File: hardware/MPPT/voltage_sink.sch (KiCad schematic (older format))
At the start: 8 parts

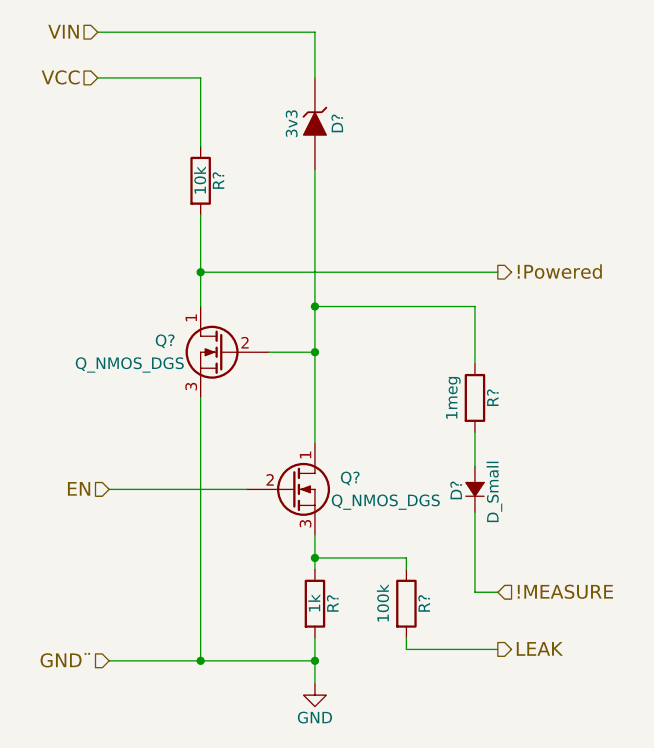
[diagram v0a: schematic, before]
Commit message: Add signaling LEDs to voltage clamps, adjust time constant on peak detect.
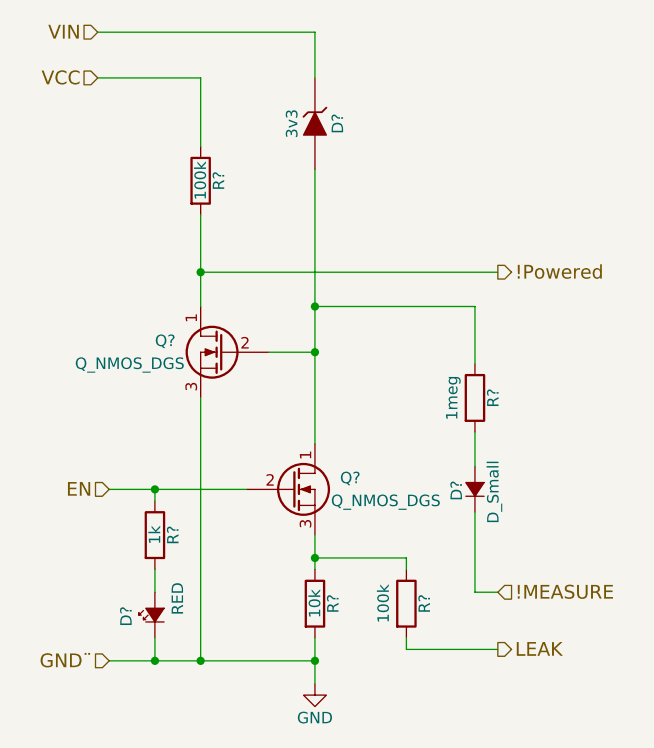
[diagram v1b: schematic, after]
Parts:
- added D?: RED, symbol Led_Small
- added R?: 1k, symbol R
- R?: value 10k -> 100k
- R?: value 1k -> 10k
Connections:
- net EN: now also R?.1
- net GND: now also D?.1 (K)
- new net: D?.2 (A), R?.2
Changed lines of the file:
@@
 $Descr A4 11693 8268
 encoding utf-8
-Sheet 6 7
+Sheet 2 7
 Title ""
 Date ""
@@
 AR Path="/55E4F9FD/55E4BF6F" Ref="D?"  Part="1"
 AR Path="/55E4FA05/55E4BF6F" Ref="D?"  Part="1"
+AR Path="/55E4E347/55E4BF6F" Ref="D?"  Part="1"
 F 0 "D?" H 3000 1650 50  0000 C CNN
 F 1 "3v3" H 3000 1450 50  0000 C CNN
@@
 AR Path="/55E4F9FD/55E4BF9E" Ref="Q?"  Part="1"
 AR Path="/55E4FA05/55E4BF9E" Ref="Q?"  Part="1"
+AR Path="/55E4E347/55E4BF9E" Ref="Q?"  Part="1"
 F 0 "Q?" H 3200 3200 50  0000 R CNN
 F 1 "Q_NMOS_DGS" H 3550 3100 50  0000 R CNN
@@
 AR Path="/55E4F9FD/55E4C1A1" Ref="#PWR?"  Part="1"
 AR Path="/55E4FA05/55E4C1A1" Ref="#PWR?"  Part="1"
+AR Path="/55E4E347/55E4C1A1" Ref="#PWR?"  Part="1"
 F 0 "#PWR?" H 3000 3750 50  0001 C CNN
 F 1 "GND" H 3000 3850 50  0000 C CNN
@@
 AR Path="/55E4F9FD/55E4C215" Ref="Q?"  Part="1"
 AR Path="/55E4FA05/55E4C215" Ref="Q?"  Part="1"
+AR Path="/55E4E347/55E4C215" Ref="Q?"  Part="1"
 F 0 "Q?" H 2900 2600 50  0000 R CNN
 F 1 "Q_NMOS_DGS" H 3250 2500 50  0000 R CNN
@@
 AR Path="/55E4F9FD/55E4C2BF" Ref="R?"  Part="1"
 AR Path="/55E4FA05/55E4C2BF" Ref="R?"  Part="1"
+AR Path="/55E4E347/55E4C2BF" Ref="R?"  Part="1"
 F 0 "R?" V 2580 1800 50  0000 C CNN
-F 1 "10k" V 2500 1800 50  0000 C CNN
+F 1 "100k" V 2500 1800 50  0000 C CNN
 F 2 "" V 2430 1800 30  0000 C CNN
 F 3 "" H 2500 1800 30  0000 C CNN
@@
 AR Path="/55E4F9FD/55E4C465" Ref="R?"  Part="1"
 AR Path="/55E4FA05/55E4C465" Ref="R?"  Part="1"
+AR Path="/55E4E347/55E4C465" Ref="R?"  Part="1"
 F 0 "R?" V 3780 2750 50  0000 C CNN
 F 1 "1meg" V 3600 2750 50  0000 C CNN
@@
 AR Path="/55E4F9FD/55E4C4D0" Ref="D?"  Part="1"
 AR Path="/55E4FA05/55E4C4D0" Ref="D?"  Part="1"
+AR Path="/55E4E347/55E4C4D0" Ref="D?"  Part="1"
 F 0 "D?" H 3650 3230 50  0000 L CNN
 F 1 "D_Small" H 3550 3070 50  0000 L CNN
@@
 AR Path="/55E4FA05/55E995FE" Ref="R?"  Part="1"
 AR Path="/55E4F9FD/55E995FE" Ref="R?"  Part="1"
+AR Path="/55E4E347/55E995FE" Ref="R?"  Part="1"
 F 0 "R?" V 3080 3650 50  0000 C CNN
-F 1 "1k" V 3000 3650 50  0000 C CNN
+F 1 "10k" V 3000 3650 50  0000 C CNN
 F 2 "" V 2930 3650 30  0000 C CNN
 F 3 "" H 3000 3650 30  0000 C CNN
@@
 AR Path="/55E4FA05/55EAD856" Ref="R?"  Part="1"
 AR Path="/55E4F9FD/55EAD856" Ref="R?"  Part="1"
+AR Path="/55E4E347/55EAD856" Ref="R?"  Part="1"
+AR Path="/55E4BF47/55EAD856" Ref="R?"  Part="1"
 F 0 "R?" V 3480 3650 50  0000 C CNN
 F 1 "100k" V 3300 3650 50  0000 C CNN
@@
 Wire Wire Line
 	3400 3850 3800 3850
+$Comp
+L Led_Small D?
+U 1 1 55F3572D
+P 2300 3700
+F 0 "D?" H 2250 3825 50  0000 L CNN
+F 1 "RED" H 2300 3600 50  0000 L CNN
+F 2 "" V 2300 3700 60  0000 C CNN
+F 3 "" V 2300 3700 60  0000 C CNN
+	1    2300 3700
+	0    -1   -1   0
+$EndComp
+$Comp
+L R R?
+U 1 1 55F35776
+P 2300 3350
+F 0 "R?" V 2380 3350 50  0000 C CNN
+F 1 "1k" V 2300 3350 50  0000 C CNN
+F 2 "" V 2230 3350 30  0000 C CNN
+F 3 "" H 2300 3350 30  0000 C CNN
+	1    2300 3350
+	1    0    0    -1
+$EndComp
+Wire Wire Line
+	2300 3150 2300 3200
+Connection ~ 2300 3150
+Wire Wire Line
+	2300 3500 2300 3600
+Wire Wire Line
+	2300 3800 2300 3900
+Connection ~ 2300 3900
 $EndSCHEMATC
